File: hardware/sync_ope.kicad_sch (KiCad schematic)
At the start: 54 parts, among them J1 rca, J10 rca, J2 barrel_jack, J3 europower, J4 mono_jack_3.5mm, J5 mono_jack_3.5mm, J6 rca, J7 diy_power_header, J8 mono_jack_3.5mm, J9 rca, U1 AD8072, U2 LM2575-5.0BT, U3 LM2575-5.0BT, U4 LT1251

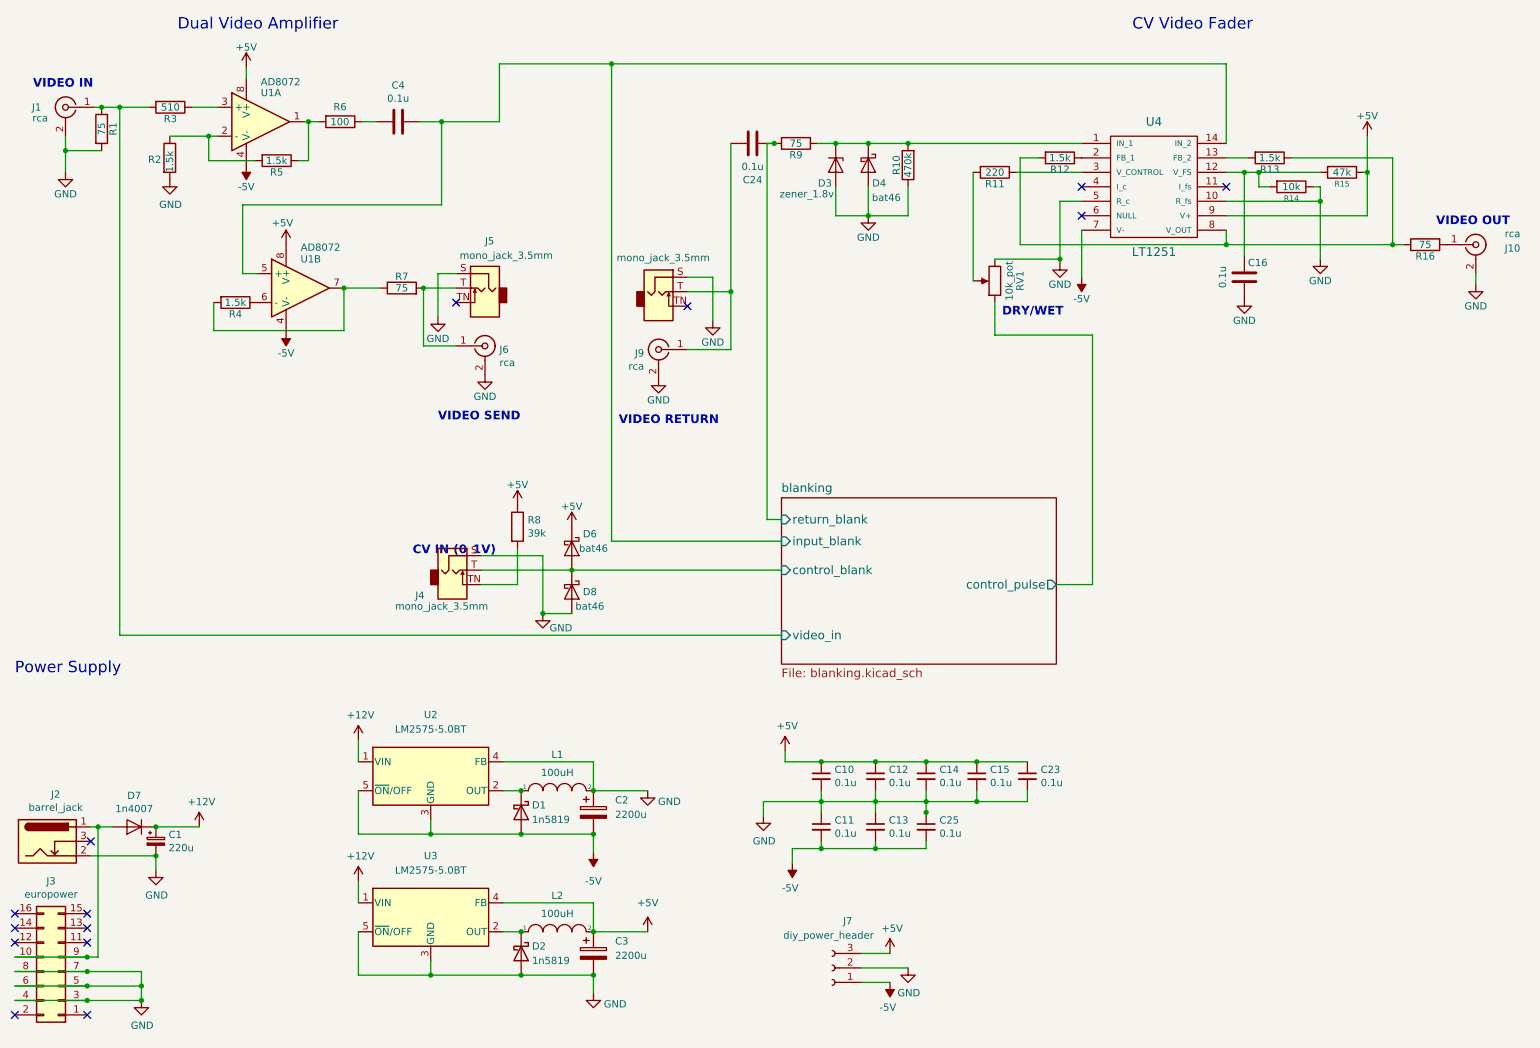
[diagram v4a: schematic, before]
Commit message: make small fixes for colour shift / level adjust
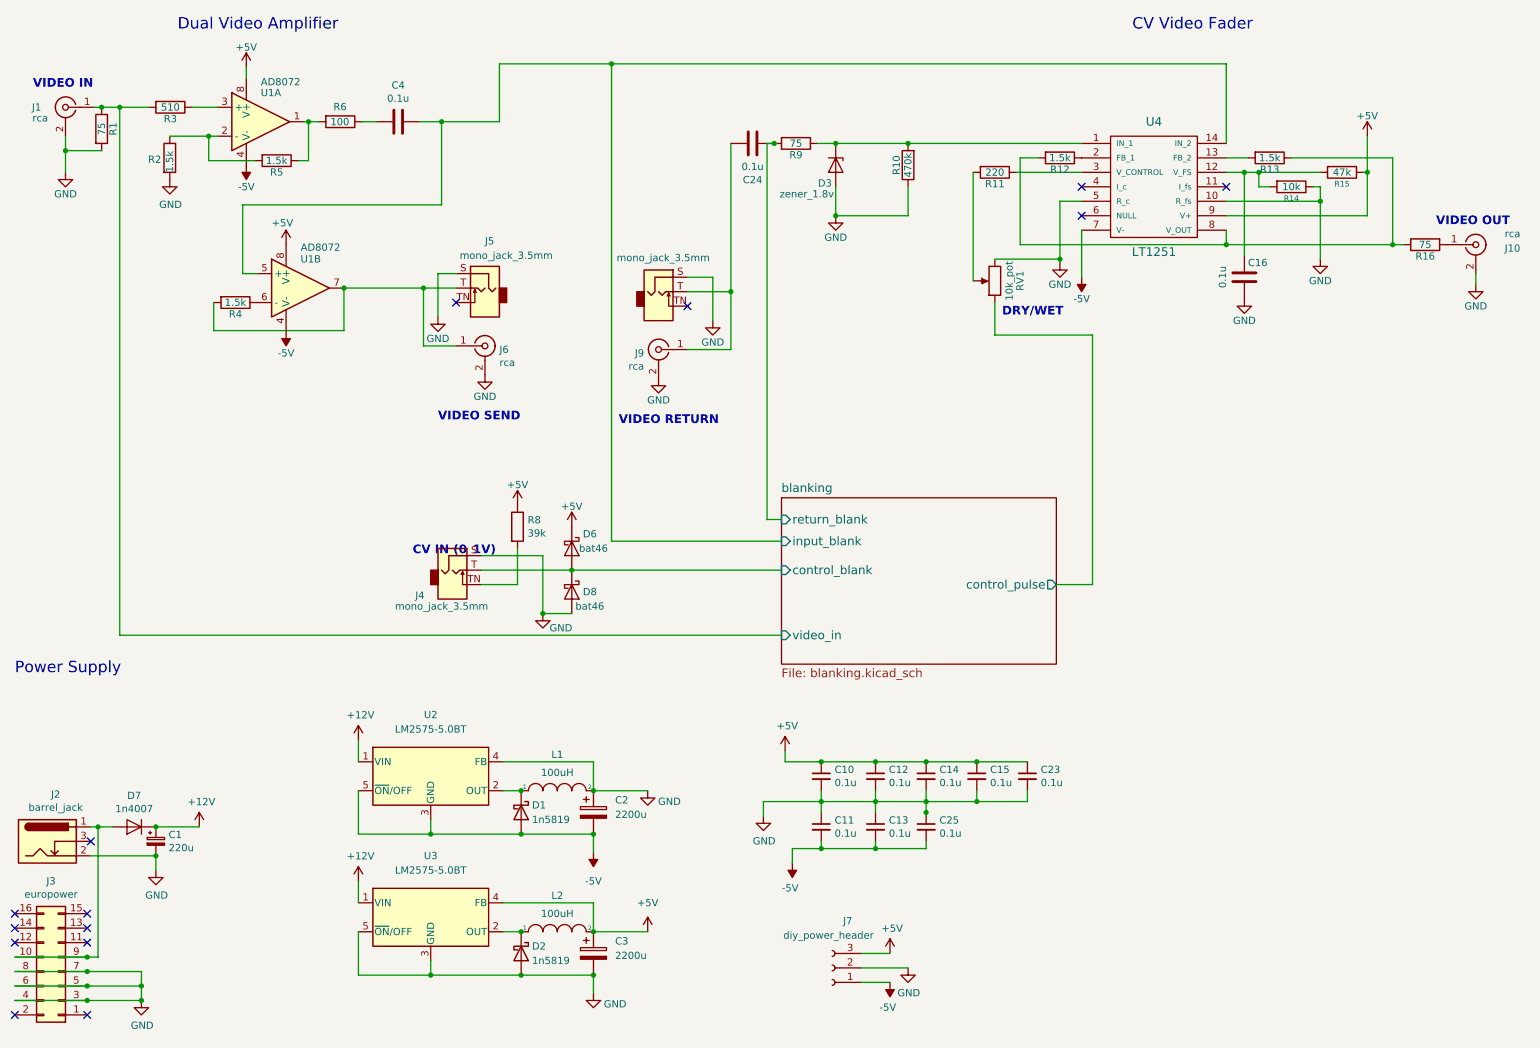
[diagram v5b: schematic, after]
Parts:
- removed D4: bat46, Diode_THT:D_DO-35_SOD27_P7.62mm_Horizontal, symbol Sync-Ope-proto-rescue:D_Schottky-Device
- removed R7: 75, Resistor_THT:R_Axial_DIN0204_L3.6mm_D1.6mm_P7.62mm_Horizontal, symbol Sync-Ope-proto-rescue:R-Sync-Ope-proto-Sync-Ope-proto-rescue
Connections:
- net at R4.2, U1.7: now also J5.T, J6.1 (In)
